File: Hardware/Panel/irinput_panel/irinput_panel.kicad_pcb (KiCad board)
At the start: 2 copper layers, 25 x 200 mm, 14 parts

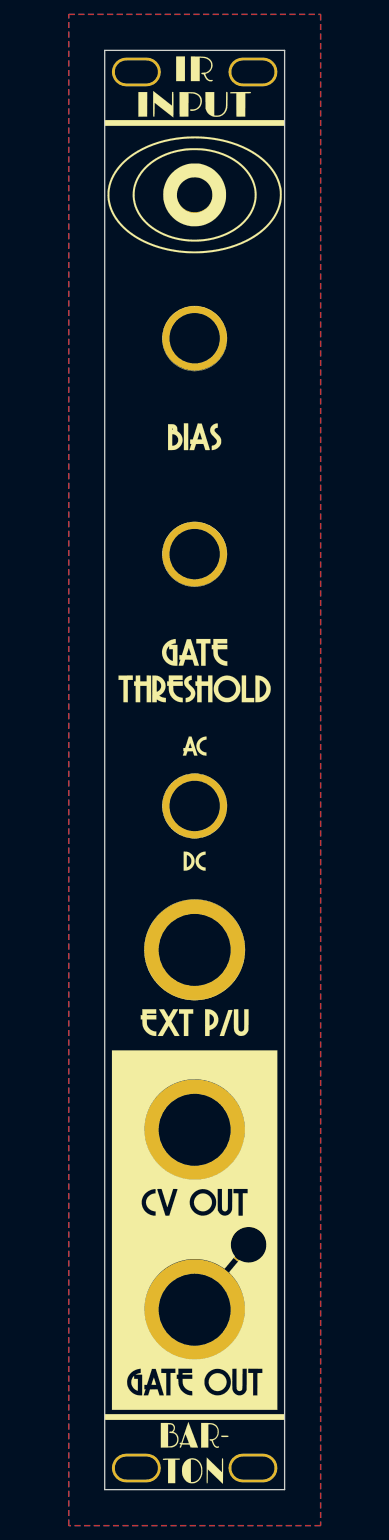
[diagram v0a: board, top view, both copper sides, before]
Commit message: Silkscreen cleanup, revised panel
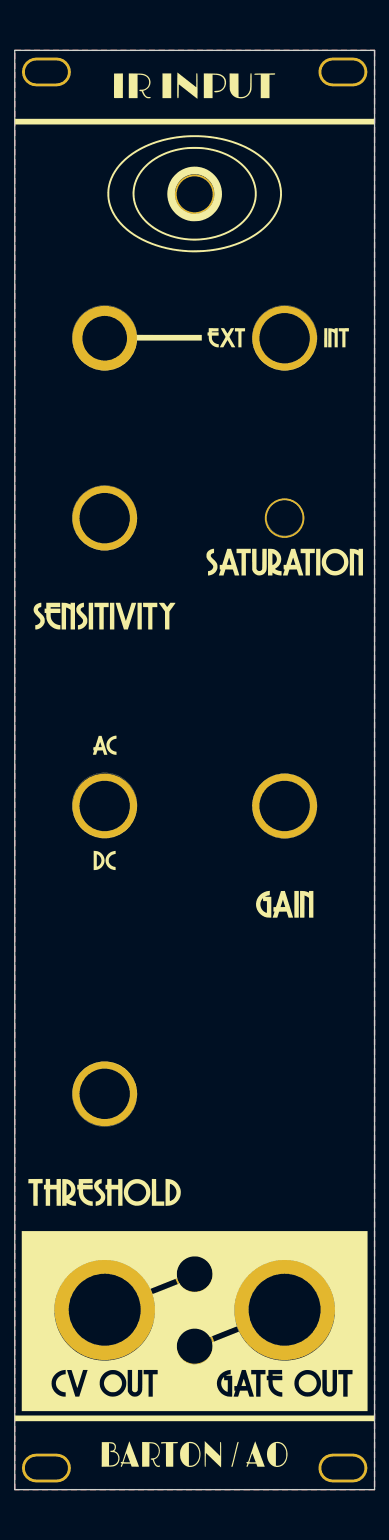
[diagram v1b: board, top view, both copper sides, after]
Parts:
- removed the H5 at (19.1, 204.6)
- removed the H8 at (38.1, 10.6)
- added H10: Led_Hole, Kosmo_panel:Kosmo_LED_Hole, F.Cu at (28.6, 177.6)
- added H11: Led_Hole, Kosmo_panel:Kosmo_LED_Hole, F.Cu at (41.1, 72.6)
- added H12: Switch_Hole, Kosmo_panel:Kosmo_Switch_Hole, F.Cu at (41.1, 47.6)
- added H13: Panel, Kosmo_panel:Kosmo_Panel_Dual_Slotted_Mounting_Holes, B.Cu at (50.6, 204.6)
- added H14: Panel, Kosmo_panel:Kosmo_Panel_Dual_Slotted_Mounting_Holes, F.Cu at (6.60, 204.6)
- added H6: Pot_Hole, Kosmo_panel:Kosmo_Pot_Hole, F.Cu at (41.1, 112.6)
- H3: renamed from H6; footprint Kosmo_panel:Kosmo_Jack_Hole -> Kosmo_panel:Little_Jack_Hole
- moved H3 85.9 mm to (16.1, 47.6)
- moved H4 76.0 mm to (16.1, 152.6)
- moved H1 28.0 mm to (16.1, 182.6)
- moved H5 28.0 mm to (16.1, 72.6)
- moved H9 15.9 mm to (28.6, 187.6)
- moved H2 12.5 mm to (41.1, 182.6)
- moved H7 12.5 mm to (16.1, 112.6)
- renumbered H9 to H5, H3 to H7, H7 to H8, H10 to H9
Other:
- board size 25 x 200 mm -> 50 x 200 mm
- net class Default removed
- board text added: "CV LED"
- board text added: "Ext PT"
- board text added: "Gain pot"
- board text added: "Int/Ext switch"
- board text added: "Panel design by Rich Holmes CC0 1.0 Feb 2022 JLCJLCJLCJLC"
- board text added: "Saturation LED"
- board text added: "Sensitivity pot"
- board text removed: "Bias pot"
- board text removed: "External pickup jack"
- board text removed: "Panel design by Rich Holmes CC0 1.0 October 2021 JLCJLCJLCJLC"
